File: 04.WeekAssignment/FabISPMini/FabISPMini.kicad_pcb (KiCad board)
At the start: 2 copper layers, 75.6 x 24.8 mm, 18 parts, among them J1 2x3Wire, J2 USB_OTG, U1 ATTINY44A-SSU

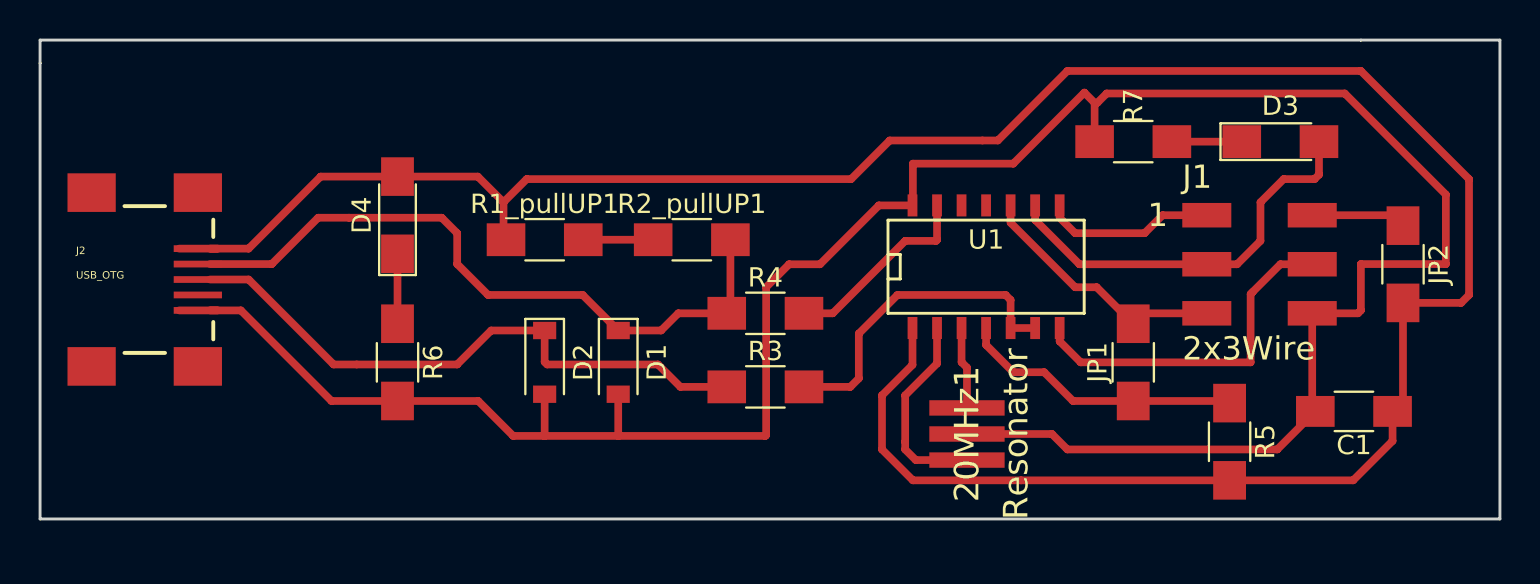
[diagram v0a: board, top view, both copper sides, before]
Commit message: Correct files to 74mm
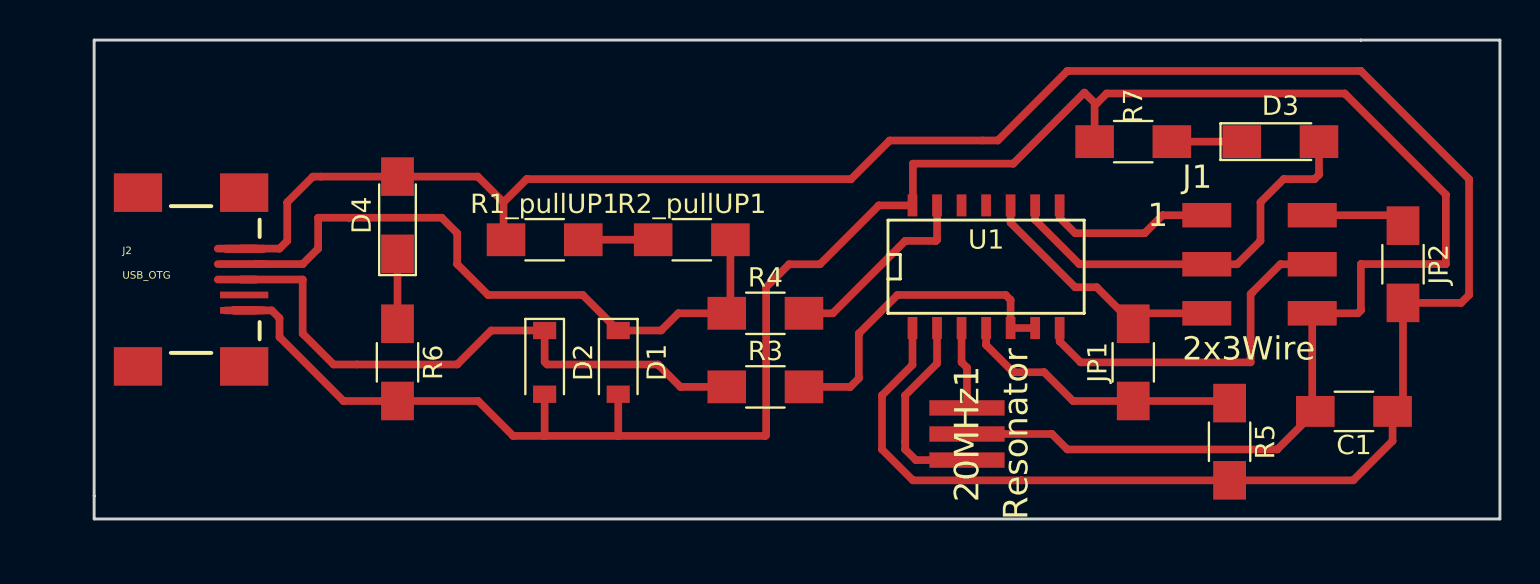
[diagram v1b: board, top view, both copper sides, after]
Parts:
- moved J2 2.40 mm to (26.4, 174.8)
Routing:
- net (no net): track 4.00 -> 6.00 mm
- net Net-(D2-Pad1): track 31.5 -> 32.7 mm
- net VCC: track 126.3 -> 127.1 mm
- net Earth: track 126.2 -> 126.7 mm
- net Net-(D1-Pad1): track 35.6 -> 36.2 mm
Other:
- board size 75.6 x 24.8 mm -> 72.8 x 24.8 mm
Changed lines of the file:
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@@
     (links 32)
     (no_connects 0)
-    (area 21.499999 161.499999 96.100001 188.500001)
+    (area 19.068399 161.499999 96.100001 188.696857)
     (thickness 1.6)
     (drawings 10)
-    (tracks 160)
+    (tracks 171)
     (zones 0)
     (modules 18)
@@
   )
   (module fab:USB_MINIB (layer F.Cu)
-    (at 24 174.8)
+    (at 26.4 174.8)
     (fp_text reference J2 (at -2.54 -1.27) (layer F.SilkS)
       (effects (font (size 0.38608 0.38608) (thickness 0.032512)) (justify left bottom))
@@
     (pad VBUS smd rect (at 3.77 -1.6) (size 2.5 0.35) (layers F.Cu F.Paste F.Mask))
   )
-  (gr_line (start 19.6 162.4) (end 88 162.4) (angle 90) (layer Edge.Cuts) (width 0.15))
-  (gr_line (start 19.6 163.6) (end 19.6 162.4) (angle 90) (layer Edge.Cuts) (width 0.15))
-  (gr_line (start 19.6 187.2) (end 19.6 163.6) (angle 90) (layer Edge.Cuts) (width 0.15))
-  (gr_line (start 95.2 187.2) (end 19.6 187.2) (angle 90) (layer Edge.Cuts) (width 0.15))
+  (gr_line (start 95.2 187.2) (end 22.4 187.2) (angle 90) (layer Edge.Cuts) (width 0.15))
+  (gr_line (start 22.4 162.4) (end 88 162.4) (angle 90) (layer Edge.Cuts) (width 0.15))
+  (gr_line (start 22.4 186) (end 22.4 187.2) (angle 90) (layer Edge.Cuts) (width 0.15))
   (gr_line (start 95.2 162.4) (end 95.2 187.2) (angle 90) (layer Edge.Cuts) (width 0.15))
+  (gr_line (start 22.4 186) (end 22.4 162.4) (angle 90) (layer Edge.Cuts) (width 0.15))
   (gr_line (start 88 162.4) (end 95.2 162.4) (angle 90) (layer Edge.Cuts) (width 0.15))
   (gr_line (start 21.6 188.4) (end 21.6 161.6) (angle 90) (layer Margin) (width 0.2))
@@
   (gr_line (start 96 161.6) (end 96 188.4) (angle 90) (layer Margin) (width 0.2))
   (gr_line (start 21.6 161.6) (end 96 161.6) (angle 90) (layer Margin) (width 0.2))
-  (segment (start 26.8 176.4) (end 28.8 176.4) (width 0.4) (layer F.Cu) (net 0) (status 30))
-  (segment (start 26.8 173.2) (end 28.8 173.2) (width 0.4) (layer F.Cu) (net 0) (status 30))
+  (segment (start 29.2 176.4) (end 31.2 176.4) (width 0.4) (layer F.Cu) (net 0) (status 30))
+  (segment (start 29.2 173.2) (end 31.2 173.2) (width 0.4) (layer F.Cu) (net 0) (status 30))
+  (segment (start 30 173.2) (end 30.8 173.2) (width 0.4) (layer F.Cu) (net 0) (status 30))
+  (segment (start 30.8 174) (end 31.2 174) (width 0.4) (layer F.Cu) (net 0) (status 30))
+  (segment (start 30 174.8) (end 30.8 174.8) (width 0.4) (layer F.Cu) (net 0) (status 30))
   (segment (start 67.6 184.15) (end 64.95 184.15) (width 0.4) (layer F.Cu) (net 1))
   (segment (start 66.05 179.15) (end 66.05 177.312) (width 0.4) (layer F.Cu) (net 1))
@@
   (segment (start 64.4 183.6) (end 64.4 183.2) (width 0.4) (layer F.Cu) (net 1))
   (segment (start 64.95 184.15) (end 64.4 183.6) (width 0.4) (layer F.Cu) (net 1))
-  (segment (start 38.11 181.09) (end 34.69 181.09) (width 0.4) (layer F.Cu) (net 2))
-  (segment (start 30 176.4) (end 28.4 176.4) (width 0.4) (layer F.Cu) (net 2))
-  (segment (start 34.69 181.09) (end 30 176.4) (width 0.4) (layer F.Cu) (net 2))
+  (segment (start 29.6 176.4) (end 30.8 176.4) (width 0.4) (layer F.Cu) (net 2) (status 30))
+  (segment (start 38.11 181.09) (end 35.31 181.09) (width 0.4) (layer F.Cu) (net 2))
+  (segment (start 31.6 176.4) (end 29.6 176.4) (width 0.4) (layer F.Cu) (net 2) (status 20))
+  (segment (start 32 176.8) (end 31.6 176.4) (width 0.4) (layer F.Cu) (net 2))
+  (segment (start 32 177.78) (end 32 176.8) (width 0.4) (layer F.Cu) (net 2))
+  (segment (start 35.31 181.09) (end 32 177.78) (width 0.4) (layer F.Cu) (net 2))
   (segment (start 72.8 183.6) (end 83.67 183.6) (width 0.4) (layer F.Cu) (net 2))
   (segment (start 67.6 182.8) (end 72 182.8) (width 0.4) (layer F.Cu) (net 2) (status 10))
@@
   (segment (start 67.6 179.36) (end 67.6 181.45) (width 0.4) (layer F.Cu) (net 3))
   (segment (start 67.32 179.08) (end 67.6 179.36) (width 0.4) (layer F.Cu) (net 3))
+  (segment (start 34.13 169.47) (end 33.73 169.47) (width 0.4) (layer F.Cu) (net 4))
   (segment (start 38.11 169.47) (end 34.13 169.47) (width 0.4) (layer F.Cu) (net 4))
-  (segment (start 30.4 173.2) (end 28.4 173.2) (width 0.4) (layer F.Cu) (net 4))
-  (segment (start 34.13 169.47) (end 30.4 173.2) (width 0.4) (layer F.Cu) (net 4))
+  (segment (start 32 173.2) (end 28.8 173.2) (width 0.4) (layer F.Cu) (net 4))
+  (segment (start 32.4 172.8) (end 32 173.2) (width 0.4) (layer F.Cu) (net 4))
+  (segment (start 32.4 170.8) (end 32.4 172.8) (width 0.4) (layer F.Cu) (net 4))
+  (segment (start 33.73 169.47) (end 32.4 170.8) (width 0.4) (layer F.Cu) (net 4))
   (segment (start 63.2 183.6) (end 64.8 185.2) (width 0.4) (layer F.Cu) (net 4))
   (segment (start 64.8 185.2) (end 70.4 185.2) (width 0.4) (layer F.Cu) (net 4))
@@
   (segment (start 42.27 169.47) (end 43.6 170.8) (width 0.4) (layer F.Cu) (net 4))
   (segment (start 43.6 172.61) (end 43.73 172.74) (width 0.4) (layer F.Cu) (net 4))
-  (segment (start 28.4 174) (end 31.6 174) (width 0.4) (layer F.Cu) (net 5))
+  (segment (start 34 171.6) (end 34 173.2) (width 0.4) (layer F.Cu) (net 5))
+  (segment (start 49.54 177.44) (end 47.7 175.6) (width 0.4) (layer F.Cu) (net 5) (status 20))
+  (segment (start 42.8 175.6) (end 47.7 175.6) (width 0.4) (layer F.Cu) (net 5))
+  (segment (start 41.2 174) (end 42.8 175.6) (width 0.4) (layer F.Cu) (net 5))
+  (segment (start 41.2 172.4) (end 41.2 174) (width 0.4) (layer F.Cu) (net 5))
+  (segment (start 40.4 171.6) (end 41.2 172.4) (width 0.4) (layer F.Cu) (net 5))
+  (segment (start 35.6 171.6) (end 40.4 171.6) (width 0.4) (layer F.Cu) (net 5))
   (segment (start 35.6 171.6) (end 34 171.6) (width 0.4) (layer F.Cu) (net 5))
-  (segment (start 35.6 171.6) (end 40.4 171.6) (width 0.4) (layer F.Cu) (net 5))
-  (segment (start 40.4 171.6) (end 41.2 172.4) (width 0.4) (layer F.Cu) (net 5))
-  (segment (start 41.2 172.4) (end 41.2 174) (width 0.4) (layer F.Cu) (net 5))
-  (segment (start 41.2 174) (end 42.8 175.6) (width 0.4) (layer F.Cu) (net 5))
-  (segment (start 42.8 175.6) (end 47.7 175.6) (width 0.4) (layer F.Cu) (net 5))
-  (segment (start 47.7 175.6) (end 49.54 177.44) (width 0.4) (layer F.Cu) (net 5) (status 20))
-  (segment (start 34 171.6) (end 31.6 174) (width 0.4) (layer F.Cu) (net 5))
+  (segment (start 33.2 174) (end 28.8 174) (width 0.4) (layer F.Cu) (net 5))
+  (segment (start 34 173.2) (end 33.2 174) (width 0.4) (layer F.Cu) (net 5))
   (segment (start 51.76 177.44) (end 52.65 176.55) (width 0.4) (layer F.Cu) (net 5))
   (segment (start 49.54 177.44) (end 51.76 177.44) (width 0.4) (layer F.Cu) (net 5) (status 10))
@@
   (segment (start 55.35 176.36) (end 55.16 176.55) (width 0.4) (layer F.Cu) (net 5))
   (segment (start 55.35 176.36) (end 55.16 176.55) (width 0.4) (layer F.Cu) (net 5))
+  (segment (start 34.8 179.2) (end 33.2 177.6) (width 0.4) (layer F.Cu) (net 6))
+  (segment (start 41.2 179.2) (end 42.96 177.44) (width 0.4) (layer F.Cu) (net 6))
+  (segment (start 45.73 177.44) (end 42.96 177.44) (width 0.4) (layer F.Cu) (net 6) (status 20))
+  (segment (start 36 179.2) (end 41.2 179.2) (width 0.4) (layer F.Cu) (net 6))
   (segment (start 36 179.2) (end 34.8 179.2) (width 0.4) (layer F.Cu) (net 6))
-  (segment (start 36 179.2) (end 41.2 179.2) (width 0.4) (layer F.Cu) (net 6))
-  (segment (start 45.73 177.44) (end 42.96 177.44) (width 0.4) (layer F.Cu) (net 6) (status 20))
-  (segment (start 41.2 179.2) (end 42.96 177.44) (width 0.4) (layer F.Cu) (net 6))
-  (segment (start 30.4 174.8) (end 28.4 174.8) (width 0.4) (layer F.Cu) (net 6))
-  (segment (start 34.8 179.2) (end 30.4 174.8) (width 0.4) (layer F.Cu) (net 6))
+  (segment (start 33.2 174.8) (end 28.8 174.8) (width 0.4) (layer F.Cu) (net 6))
+  (segment (start 33.2 177.6) (end 33.2 174.8) (width 0.4) (layer F.Cu) (net 6))
   (segment (start 45.73 177.44) (end 45.73 179.07) (width 0.4) (layer F.Cu) (net 6) (status 10))
   (segment (start 52.76 180.36) (end 55.16 180.36) (width 0.4) (layer F.Cu) (net 6))
